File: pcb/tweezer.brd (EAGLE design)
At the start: 20 x 26 mm, 33 parts, among them IC1 AD7995, IC2 TS507CLT, IC3 TS507CLT, IC5 ESDA6V1SC5, IC6 AT24CS04-SOT23

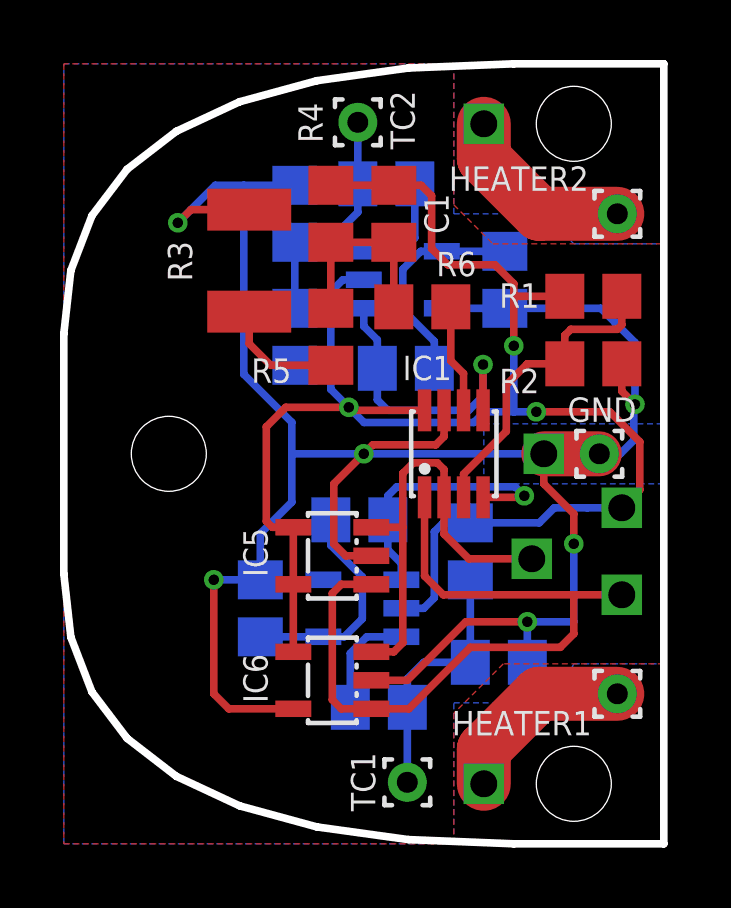
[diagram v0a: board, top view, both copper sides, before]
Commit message: fixing op amp (iron,tweezer)
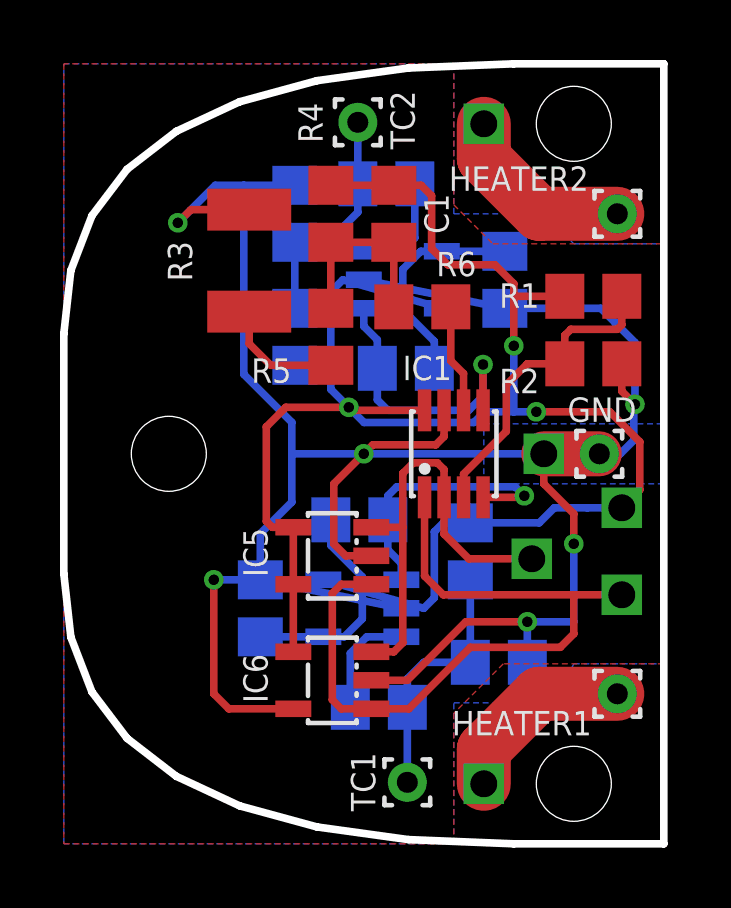
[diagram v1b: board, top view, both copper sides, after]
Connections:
- net +5V: now also IC2.5, IC3.5; no longer IC2.2, IC3.2
- net GND: now also IC2.2, IC3.2; no longer IC2.5, IC3.5
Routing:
- net +5V: track 57.8 -> 63.3 mm
- net GND: track 78.5 -> 83.9 mm
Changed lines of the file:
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@@
 <attribute name="VALUE" x="5.16" y="19.73" size="1.27" layer="28" rot="MR90"/>
 </element>
-<element name="IC2" library="solderpi" library_urn="urn:adsk.eagle:library:1437534" package="SOT23-5L" package3d_urn="urn:adsk.eagle:package:1437676/5" value="TS507CLT" x="9.95" y="7.85" smashed="yes" rot="MR270">
+<element name="IC2" library="solderpi" library_urn="urn:adsk.eagle:library:1437534" package="SOT23-5L" package3d_urn="urn:adsk.eagle:package:1437676/7" value="TS507CLT" x="9.95" y="7.85" smashed="yes" rot="MR270">
 <attribute name="NAME" x="7.455" y="10.155" size="0.8128" layer="26" rot="MR0"/>
 <attribute name="VALUE" x="13.379" y="9.755" size="1.27" layer="28" rot="MR270"/>
 </element>
-<element name="IC3" library="solderpi" library_urn="urn:adsk.eagle:library:1437534" package="SOT23-5L" package3d_urn="urn:adsk.eagle:package:1437676/5" value="TS507CLT" x="11.3" y="18.8" smashed="yes" rot="MR90">
+<element name="IC3" library="solderpi" library_urn="urn:adsk.eagle:library:1437534" package="SOT23-5L" package3d_urn="urn:adsk.eagle:package:1437676/7" value="TS507CLT" x="11.3" y="18.8" smashed="yes" rot="MR90">
 <attribute name="NAME" x="14.505" y="20.955" size="0.8128" layer="26" rot="MR0"/>
 <attribute name="VALUE" x="7.871" y="16.895" size="1.27" layer="28" rot="MR90"/>
@@
 <attribute name="VALUE" x="12.16" y="18.165" size="1.27" layer="28" rot="MR90"/>
 </element>
-<element name="R2" library="solderpi" library_urn="urn:adsk.eagle:library:1437534" package="R0805" package3d_urn="urn:adsk.eagle:package:1581953/3" value="330k @25°C, 1%, ß=3930" x="17.65" y="16" smashed="yes" rot="R180">
+<element name="R2" library="solderpi" library_urn="urn:adsk.eagle:library:1437534" package="R0805" package3d_urn="urn:adsk.eagle:package:1581953/4" value="330k @25°C, 1%, ß=3930" x="17.65" y="16" smashed="yes" rot="R180">
 <attribute name="NAME" x="14.515" y="15.02" size="0.8128" layer="25"/>
 <attribute name="VALUE" x="18.285" y="18.54" size="1.27" layer="27" rot="R180"/>
@@
 </element>
 <element name="ß" library="solderpi" library_urn="urn:adsk.eagle:library:1437534" package="WIREPAD" package3d_urn="urn:adsk.eagle:package:1593774/7" value="WIREPAD" x="14" y="2" smashed="yes"/>
-<element name="IC5" library="solderpi" library_urn="urn:adsk.eagle:library:1437534" package="SOT23-5L" package3d_urn="urn:adsk.eagle:package:1437676/5" value="ESDA6V1SC5" x="8.95" y="9.6" smashed="yes" rot="R90">
+<element name="IC5" library="solderpi" library_urn="urn:adsk.eagle:library:1437534" package="SOT23-5L" package3d_urn="urn:adsk.eagle:package:1437676/7" value="ESDA6V1SC5" x="8.95" y="9.6" smashed="yes" rot="R90">
 <attribute name="NAME" x="6.795" y="8.895" size="0.8128" layer="25" rot="R90"/>
 <attribute name="VALUE" x="12.379" y="7.695" size="1.27" layer="27" rot="R90"/>
 </element>
-<element name="IC6" library="solderpi" library_urn="urn:adsk.eagle:library:1437534" package="SOT23-5L" package3d_urn="urn:adsk.eagle:package:1437676/5" value="AT24CS04-SOT23" x="8.95" y="5.45" smashed="yes" rot="R90">
+<element name="IC6" library="solderpi" library_urn="urn:adsk.eagle:library:1437534" package="SOT23-5L" package3d_urn="urn:adsk.eagle:package:1437676/7" value="AT24CS04-SOT23" x="8.95" y="5.45" smashed="yes" rot="R90">
 <attribute name="NAME" x="6.795" y="4.695" size="0.8128" layer="25" rot="R90"/>
 <attribute name="VALUE" x="12.379" y="3.545" size="1.27" layer="27" rot="R90"/>
@@
 <contactref element="R3" pad="P$1"/>
 <contactref element="R10" pad="1"/>
-<contactref element="IC2" pad="5"/>
+<contactref element="IC2" pad="2"/>
 <contactref element="C2" pad="2"/>
 <contactref element="R14" pad="1"/>
-<contactref element="IC3" pad="5"/>
+<contactref element="IC3" pad="2"/>
 <contactref element="C3" pad="2"/>
 <contactref element="IC1" pad="7"/>
-<wire x1="8.65" y1="8.8" x2="6.55" y2="8.8" width="0.254" layer="16"/>
-<wire x1="12.6" y1="17.85" x2="14.7" y2="17.85" width="0.254" layer="16"/>
+<wire x1="11.25" y1="7.85" x2="6.55" y2="8.8" width="0.254" layer="16"/>
+<wire x1="10" y1="18.8" x2="14.7" y2="17.85" width="0.254" layer="16"/>
 <wire x1="6.55" y1="8.8" x2="6.55" y2="10.34" width="0.254" layer="16"/>
 <wire x1="6.18" y1="21.14" x2="4.24" y2="21.14" width="0.254" layer="1"/>
@@
 <contactref element="R4" pad="2"/>
 <contactref element="R9" pad="2"/>
-<contactref element="IC2" pad="2"/>
+<contactref element="IC2" pad="5"/>
 <contactref element="R13" pad="2"/>
-<contactref element="IC3" pad="2"/>
+<contactref element="IC3" pad="5"/>
 <contactref element="IC1" pad="8"/>
 <wire x1="13.55" y1="10.7" x2="12.65" y2="10.7" width="0.254" layer="16"/>
@@
 <wire x1="12.35" y1="10.4" x2="12.35" y2="8.2" width="0.254" layer="16"/>
 <wire x1="12.35" y1="8.2" x2="12" y2="7.85" width="0.254" layer="16"/>
-<wire x1="12" y1="7.85" x2="11.25" y2="7.85" width="0.254" layer="16"/>
+<wire x1="12" y1="7.85" x2="8.65" y2="8.8" width="0.254" layer="16"/>
 <wire x1="9.3" y1="18.8" x2="8.9" y2="18.4" width="0.254" layer="16"/>
-<wire x1="9.3" y1="18.8" x2="10" y2="18.8" width="0.254" layer="16"/>
+<wire x1="9.3" y1="18.8" x2="12.6" y2="17.85" width="0.254" layer="16"/>
 <wire x1="8.9" y1="21.95" x2="11" y2="21.95" width="0.254" layer="1"/>
 <wire x1="13.55" y1="10.7" x2="15.85" y2="10.7" width="0.254" layer="16"/>

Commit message: parts reworked
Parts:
- C1: value 100n -> 100pF; device rcl:C0805 -> common:C0603
- C2, C3: value (none) -> 10nF; device rcl:C0805 -> common:C0603
- R1: value (none) -> 20k 0,1%; device rcl:R0805 -> common:R0603
- R10, R11, R12, R13, R14, R6, R7, R8, R9: device rcl:R0805 -> common:R0603
- R2: value 330k @25°C, 1%, ß=3930 -> 68k @25°C, 1%, ß=3985 K; device solderpi:R0805 -> common:R0603
- R4: value 200k -> 5,1M; device rcl:R0805 -> common:R0603
- R5: value 100k -> 1k; device rcl:R0805 -> common:R0603
- moved U$10 15.9 mm to (4.00, 4.80)
- moved 21 15.6 mm to (3.00, 8.60)
- moved U$9 12.9 mm to (3.00, 6.70)
- moved R3 11.8 mm to (17.8, 17.2)
- moved R1 8.90 mm to (16.4, 9.45), turned to 270 degrees
- moved R2 7.08 mm to (14.9, 9.45), turned to 90 degrees
- moved R5 6.23 mm to (15.1, 17.2)
- moved R9 5.62 mm to (10.1, 5.35)
- moved R14 4.85 mm to (11.9, 14.8), turned to 0 degrees
- moved R4 4.65 mm to (11.6, 17.2), turned to 270 degrees
- moved R13 4.41 mm to (10.2, 20.5)
- moved C1 3.88 mm to (10.2, 17.2), turned to 90 degrees
- moved IC6 3.72 mm to (11.9, 7.65), turned to 270 degrees
- moved R10 3.67 mm to (8.35, 11.1), turned to 180 degrees
- moved U$7 3.61 mm to (16.0, 21.0)
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- renumbered HEATER1 to PWR1
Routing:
- net GND: track 83.9 -> 58.4 mm
- net +5V: track 63.3 -> 48.7 mm, vias 3 -> 5
- net SCL: track 24.9 -> 12.3 mm
- net AD_COMP: track 10.5 -> 4.41 mm
- net HEATER_1: track 6.37 -> 2.45 mm
- net HEATER_2: track 6.37 -> 2.45 mm
- net TC_1: track 8.53 -> 5.44 mm
- net AD_TC_1: track 9.18 -> 6.50 mm
- net AD_TC_2: track 9.68 -> 11.9 mm
- net THERMO_FIL_TC_1: track 3.73 -> 1.50 mm
- net THERMO_FIL1: track 3.69 -> 1.50 mm
- net TC_2: track 7.71 -> 5.71 mm
- net MOTION_FIL: track 6.49 -> 4.92 mm
- net AD_MOTION: track 3.63 -> 2.22 mm
- net MOTION_DIV: track 4.09 -> 2.90 mm
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- added copper zone on layer 1, net GND
- removed copper zone on layer 1, net +5V
- removed copper zone on layer 1, net HEATER_1
- removed copper zone on layer 1, net HEATER_2
